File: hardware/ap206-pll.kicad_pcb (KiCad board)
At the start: 2 copper layers, 120 x 59 mm, 35 parts, among them CON1 AVR-ISP-6, J1 Screw_Terminal_01x06, J2 Screw_Terminal_01x05, SW1 QLOCK, U1 4069, U2 LM7805_TO220, U4 ATTINY25-20PU, U6 4504, U7 4046, Y1 11.0592

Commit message: Initial tested and working version, with fixes
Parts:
- SW1: footprint Button_Switch_THT:SW_E-Switch_EG1271_DPDT -> Button_Switch_THT:SW_CuK_JS202011CQN_DPDT_Straight
- moved RV1 4.73 mm to (74.5, 69.8)
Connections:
- J2 pad 1: /13(GRY) -> /12(WHTBLK)
- J2 pad 2: /12(WHTBLK) -> /13(GRY)
- SW1 pad 2: /12(WHTBLK) -> /13(GRY)
- SW1 pad 3: /13(GRY) -> /12(WHTBLK)
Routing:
- net +7.5V: track 142.7 -> 147.5 mm
- net /13(GRY): track 24.6 -> 20.7 mm
- net /12(WHTBLK): track 20.7 -> 24.6 mm
- net Net-(C6-Pad1): track 40.9 -> 37.4 mm
- net /19(WHT): track 20.7 -> 20.0 mm

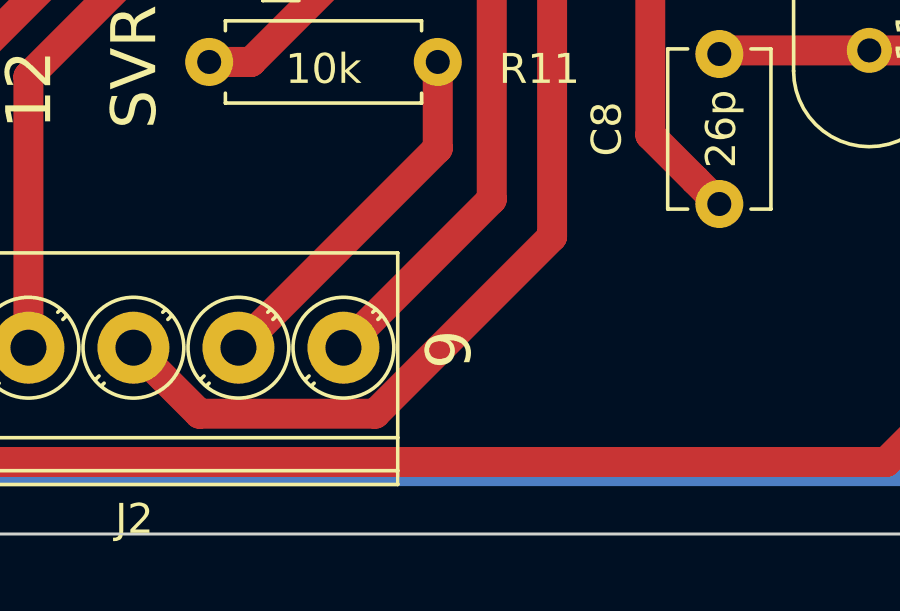
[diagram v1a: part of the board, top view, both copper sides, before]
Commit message: Add README Fix pin label
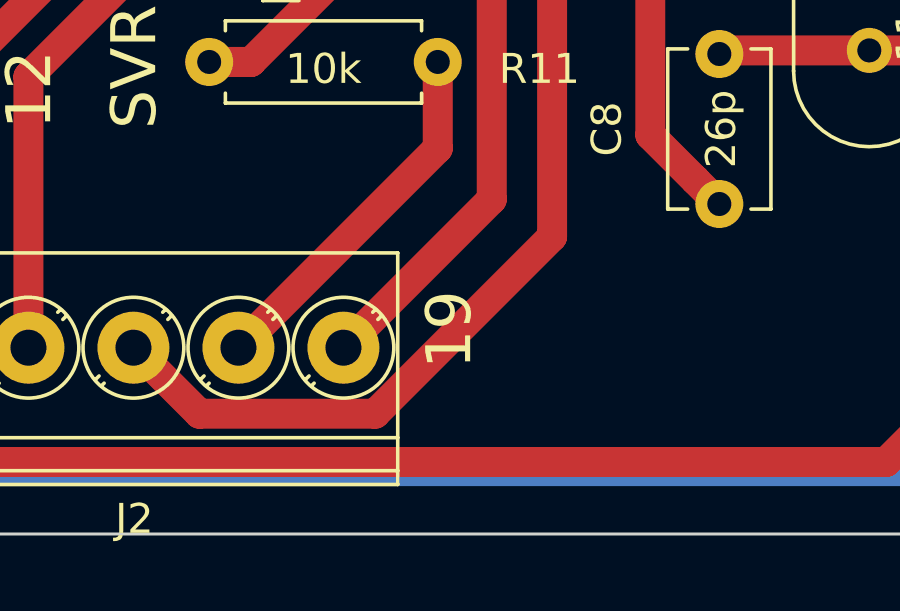
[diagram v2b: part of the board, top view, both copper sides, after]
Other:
- board text added: "19"
- board text removed: "9"
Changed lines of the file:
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@@
     (effects (font (size 1.5 1.5) (thickness 0.3)) (justify left))
   )
-  (gr_text 9 (at 95 98.5 90) (layer F.SilkS)
+  (gr_text 19 (at 95 98.5 90) (layer F.SilkS)
     (effects (font (size 1.5 1.5) (thickness 0.3)) (justify left))
   )
